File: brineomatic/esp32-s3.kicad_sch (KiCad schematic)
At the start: 27 parts, among them J19 USB_TYPE_C_16PIN, SW1 RESET, SW2 BOOT, U5 ESP32-S3-WROOM-1-N16R8, U6 USBLC6-2SC6, U7 SN74LV1T34DBV, U8 XC6210B332MR

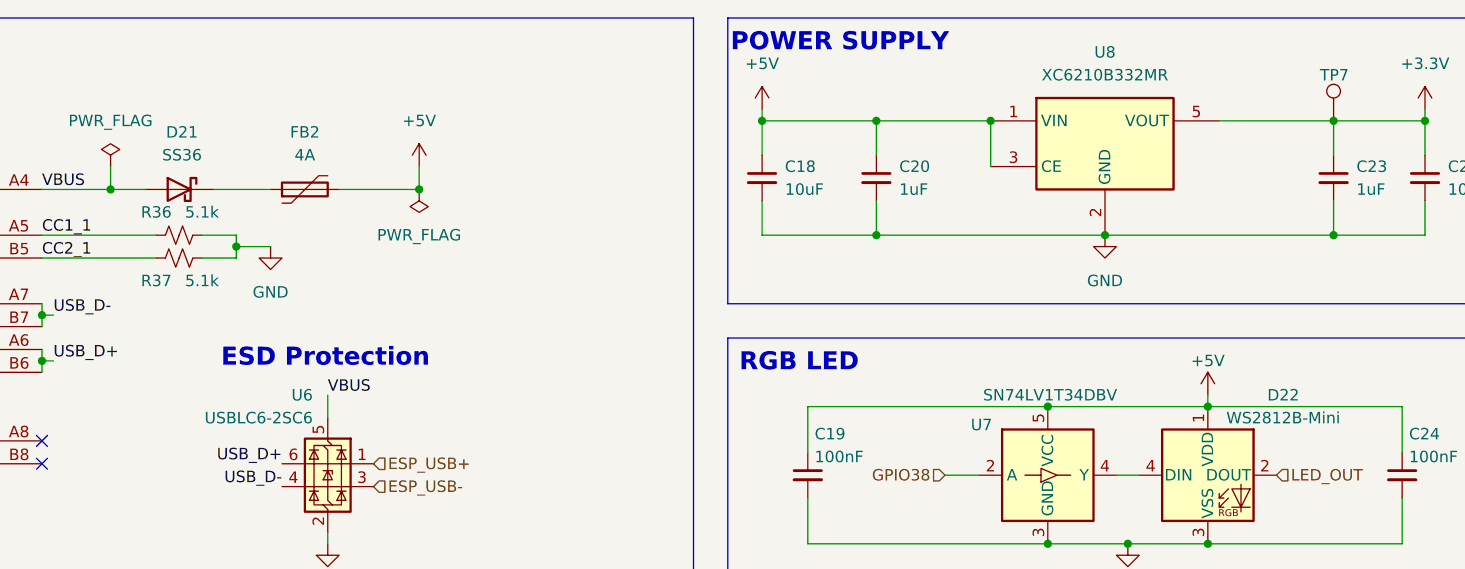
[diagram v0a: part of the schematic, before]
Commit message: more esd protection, drc passing, silkscreen fixed
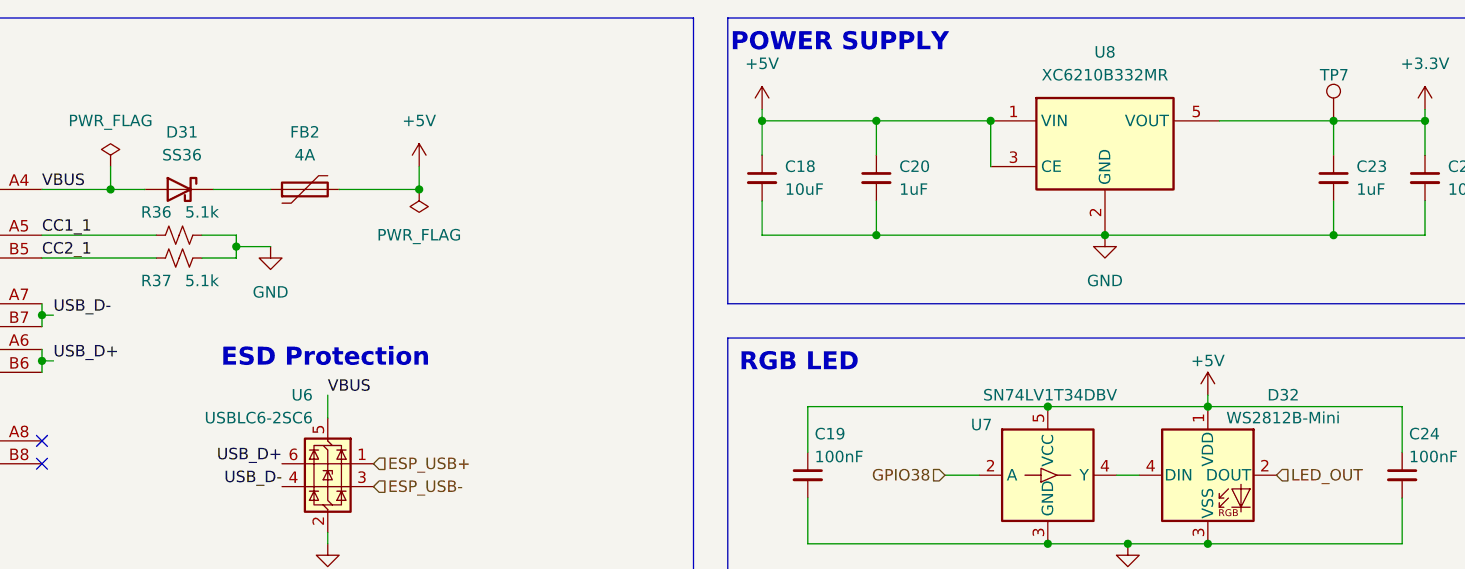
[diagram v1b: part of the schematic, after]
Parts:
- renumbered D21 to D31, D22 to D32
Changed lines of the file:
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@@
 		(on_board yes)
 		(dnp no)
-		(property "Reference" "D21"
+		(property "Reference" "D31"
 			(at 99.3775 29.21 0)
 			(effects
@@
 			(project "brineomatic"
 				(path "/96477ae2-ef08-48f3-8dd4-fe4478541f68/602af921-0504-453c-a784-e82800e98f4c"
-					(reference "D21")
+					(reference "D31")
 					(unit 1)
 				)
@@
 		(on_board yes)
 		(dnp no)
-		(property "Reference" "D22"
+		(property "Reference" "D32"
 			(at 221.742 58.42 0)
 			(effects
@@
 			(project "brineomatic"
 				(path "/96477ae2-ef08-48f3-8dd4-fe4478541f68/602af921-0504-453c-a784-e82800e98f4c"
-					(reference "D22")
-					(unit 1)
-				)
+					(reference "D32")
+					(unit 1)
+				)

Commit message: small cleanups on schematic
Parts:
- C21: value 4.7uF -> 1uF
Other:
- moved on the sheet: C18, C19, C20, C21, C22, C23, C24, C25, D32, R38, R39, SW1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

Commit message: added back up usb serial converter headers
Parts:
- added J20: Conn_01x04, Connector_PinHeader_2.54mm:PinHeader_1x04_P2.54mm_Vertical_SMD_Pin1Left, symbol Connector_Generic:Conn_01x04
- renumbered C22 to C21, C21 to C22, R39 to R38, R38 to R39, SW2 to SW1, SW1 to SW2, TP6 to TP5, TP5 to TP6
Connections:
- net +3.3V: now also J20.1 (Pin_1)
- net ESP_RXD0: now also J20.4 (Pin_4)
- net ESP_TXD0: now also J20.3 (Pin_3)
- net GND: now also J20.2 (Pin_2)
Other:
- note added: "Backup Serial Header"

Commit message: added missing gnd test point
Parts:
- renumbered TP5 to TP6, TP6 to TP7, TP7 to TP8
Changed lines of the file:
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@@
 		(on_board yes)
 		(dnp no)
-		(property "Reference" "TP7"
+		(property "Reference" "TP8"
 			(at 225.806 24.13 0)
 			(effects
@@
 			(project "brineomatic"
 				(path "/96477ae2-ef08-48f3-8dd4-fe4478541f68/602af921-0504-453c-a784-e82800e98f4c"
-					(reference "TP7")
+					(reference "TP8")
 					(unit 1)
 				)
@@
 		(on_board yes)
 		(dnp no)
-		(property "Reference" "TP6"
+		(property "Reference" "TP7"
 			(at 214.376 118.11 0)
 			(effects
@@
 			(project "brineomatic"
 				(path "/96477ae2-ef08-48f3-8dd4-fe4478541f68/602af921-0504-453c-a784-e82800e98f4c"
-					(reference "TP6")
+					(reference "TP7")
 					(unit 1)
 				)
@@
 		(on_board yes)
 		(dnp no)
-		(property "Reference" "TP5"
+		(property "Reference" "TP6"
 			(at 177.546 118.11 0)
 			(effects
@@
 			(project "brineomatic"
 				(path "/96477ae2-ef08-48f3-8dd4-fe4478541f68/602af921-0504-453c-a784-e82800e98f4c"
-					(reference "TP5")
-					(unit 1)
-				)
+					(reference "TP6")
+					(unit 1)
+				)

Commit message: added more esd protection to the power rails (24v, 5v, 3.3v)
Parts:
- added D36: SMAJ3.3A, Diode_SMD:D_SMA, symbol Device:D_TVS
- renumbered C23 to C22, C22 to C23, C25 to C24, C24 to C25, D31 to D34, D32 to D35
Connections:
- net +3.3V: now also D36.2 (A2)
- net GND: now also D36.1 (A1)
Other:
- moved on the sheet: C22, C24, TP8

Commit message: switched to the LDL1117 ldo
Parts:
- removed C18: 10uF, Capacitor_SMD:C_0603_1608Metric, symbol Device:C_Small
- removed C22: 1uF, Capacitor_SMD:C_0603_1608Metric, symbol Device:C_Small
- removed U8: XC6210B332MR, Package_TO_SOT_SMD:SOT-23-5, symbol Regulator_Linear:XC6210B332MR
- added U8: LDL1117S33R, Package_TO_SOT_SMD:SOT-223-3_TabPin2, symbol Regulator_Linear:AMS1117-3.3
- C23: renamed from C24; value 10uF -> 4.7uF
- renumbered C16 to C15, C17 to C16, C19 to C18, C20 to C19, C21 to C20, C23 to C22, C25 to C24, D34 to D33, D35 to D34, D36 to D35, R36 to R35, R37 to R36, R38 to R37, R39 to R38
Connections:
- net +3.3V: now also U8.2 (VO)
- net +5V: now also U8.3 (VI)
- net GND: now also U8.1 (GND)
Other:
- moved on the sheet: C19, C23, D35, TP8

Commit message: switch to rt7272b for 24v -> 5v regulator
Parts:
- added D34: GREEN, LED_SMD:LED_0603_1608Metric, symbol Device:LED
- added R42: 5.1k, Resistor_SMD:R_0603_1608Metric, symbol Device:R_Small_US
- D31: renamed from D33; value SS36 -> SS34; LCSC C16015 -> C8678
- renumbered C15 to C17, C16 to C18, C18 to C19, C19 to C20, C20 to C21, C23 to C22, C22 to C23, D34 to D32, D35 to D33, FB2 to FB1, R35 to R38, R36 to R39, R37 to R40, R38 to R41, TP6 to TP7, TP7 to TP9, U8 to U7, U7 to U8
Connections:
- net +3.3V: now also D34.2 (A)
- net GND: now also R42.2
- new net: D34.1 (K), R42.1
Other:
- moved on the sheet: C20, C22, D33, TP8, U7

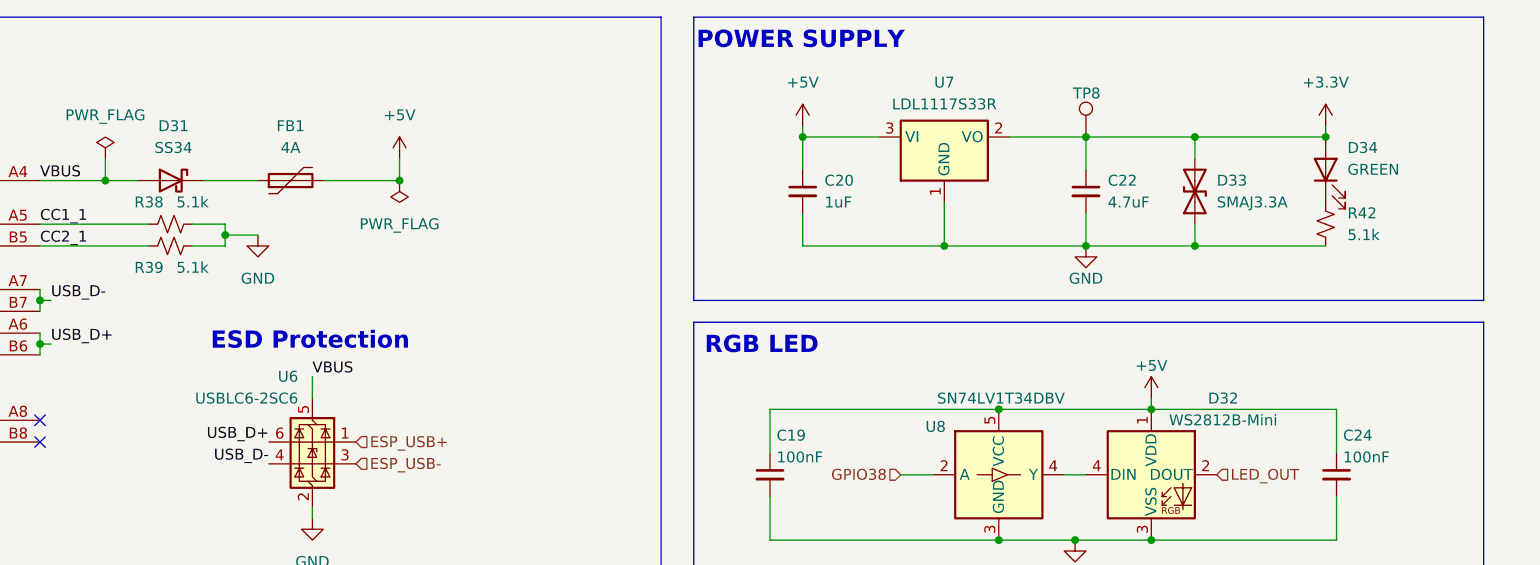
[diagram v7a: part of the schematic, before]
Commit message: added bootstrap diode just in case
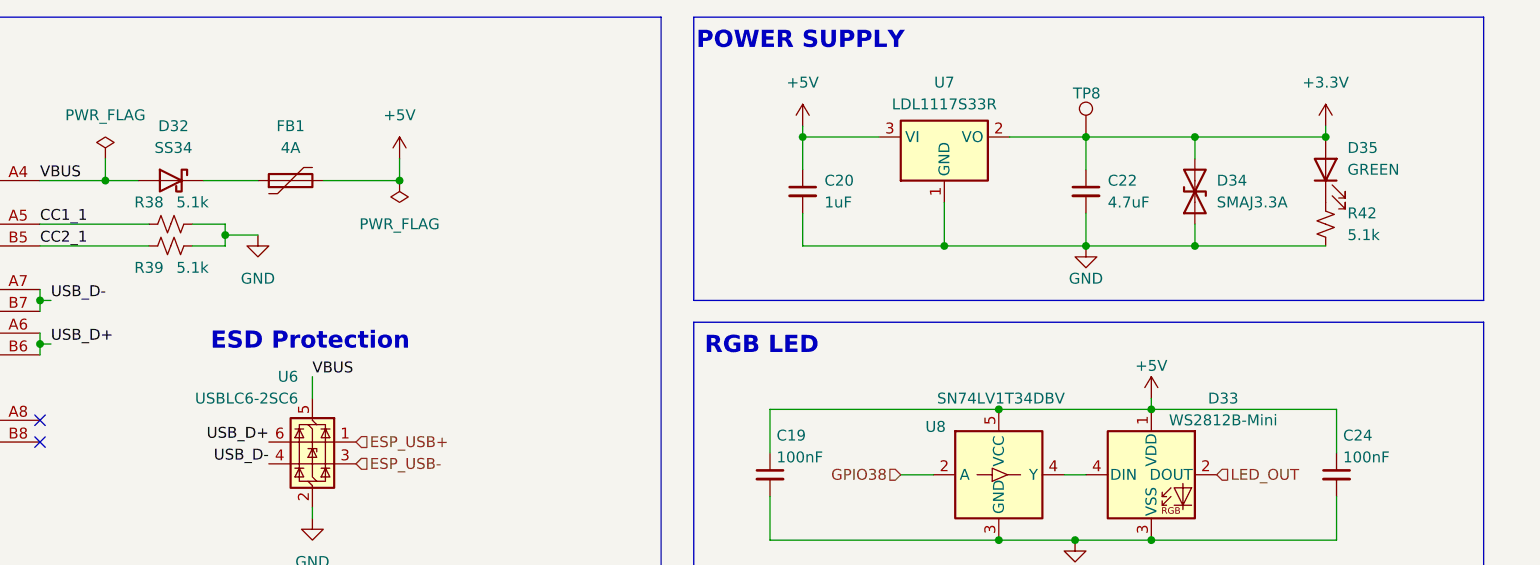
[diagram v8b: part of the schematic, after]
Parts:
- renumbered D31 to D32, D32 to D33, D33 to D34, D34 to D35
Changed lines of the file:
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@@
 		(on_board yes)
 		(dnp no)
-		(property "Reference" "#PWR045"
+		(property "Reference" "#PWR046"
 			(at 97.79 179.07 0)
 			(effects
@@
 			(project "brineomatic"
 				(path "/96477ae2-ef08-48f3-8dd4-fe4478541f68/602af921-0504-453c-a784-e82800e98f4c"
-					(reference "#PWR045")
+					(reference "#PWR046")
 					(unit 1)
 				)
@@
 		(on_board yes)
 		(dnp no)
-		(property "Reference" "#PWR057"
+		(property "Reference" "#PWR058"
 			(at 220.98 119.38 0)
 			(effects
@@
 			(project "brineomatic"
 				(path "/96477ae2-ef08-48f3-8dd4-fe4478541f68/602af921-0504-453c-a784-e82800e98f4c"
-					(reference "#PWR057")
+					(reference "#PWR058")
 					(unit 1)
 				)
@@
 		(on_board yes)
 		(dnp no)
-		(property "Reference" "D33"
+		(property "Reference" "D34"
 			(at 220.98 35.56 90)
 			(effects
@@
 			(project "brineomatic"
 				(path "/96477ae2-ef08-48f3-8dd4-fe4478541f68/602af921-0504-453c-a784-e82800e98f4c"
-					(reference "D33")
+					(reference "D34")
 					(unit 1)
 				)
@@
 		(dnp no)
 		(fields_autoplaced yes)
-		(property "Reference" "#PWR049"
+		(property "Reference" "#PWR050"
 			(at 115.57 81.28 0)
 			(effects
@@
 			(project "brineomatic"
 				(path "/96477ae2-ef08-48f3-8dd4-fe4478541f68/602af921-0504-453c-a784-e82800e98f4c"
-					(reference "#PWR049")
+					(reference "#PWR050")
 					(unit 1)
 				)
@@
 		(on_board yes)
 		(dnp no)
-		(property "Reference" "#PWR051"
+		(property "Reference" "#PWR052"
 			(at 172.72 33.02 0)
 			(effects
@@
 			(project "brineomatic"
 				(path "/96477ae2-ef08-48f3-8dd4-fe4478541f68/602af921-0504-453c-a784-e82800e98f4c"
-					(reference "#PWR051")
+					(reference "#PWR052")
 					(unit 1)
 				)
@@
 		(on_board yes)
 		(dnp no)
-		(property "Reference" "#PWR056"
+		(property "Reference" "#PWR057"
 			(at 213.36 64.77 0)
 			(effects
@@
 			(project "brineomatic"
 				(path "/96477ae2-ef08-48f3-8dd4-fe4478541f68/602af921-0504-453c-a784-e82800e98f4c"
-					(reference "#PWR056")
+					(reference "#PWR057")
 					(unit 1)
 				)
@@
 		(on_board yes)
 		(dnp no)
-		(property "Reference" "#PWR052"
+		(property "Reference" "#PWR053"
 			(at 184.15 119.38 0)
 			(effects
@@
 			(project "brineomatic"
 				(path "/96477ae2-ef08-48f3-8dd4-fe4478541f68/602af921-0504-453c-a784-e82800e98f4c"
-					(reference "#PWR052")
+					(reference "#PWR053")
 					(unit 1)
 				)
@@
 		(dnp no)
 		(fields_autoplaced yes)
-		(property "Reference" "#PWR046"
+		(property "Reference" "#PWR047"
 			(at 97.79 186.69 0)
 			(effects
@@
 			(project "brineomatic"
 				(path "/96477ae2-ef08-48f3-8dd4-fe4478541f68/602af921-0504-453c-a784-e82800e98f4c"
-					(reference "#PWR046")
+					(reference "#PWR047")
 					(unit 1)
 				)
@@
 		(dnp no)
 		(fields_autoplaced yes)
-		(property "Reference" "#PWR044"
+		(property "Reference" "#PWR045"
 			(at 85.09 162.56 0)
 			(effects
@@
 			(project "brineomatic"
 				(path "/96477ae2-ef08-48f3-8dd4-fe4478541f68/602af921-0504-453c-a784-e82800e98f4c"
-					(reference "#PWR044")
+					(reference "#PWR045")
 					(unit 1)
 				)
@@
 		(dnp no)
 		(fields_autoplaced yes)
-		(property "Reference" "#PWR054"
+		(property "Reference" "#PWR055"
 			(at 204.47 83.82 0)
 			(effects
@@
 			(project "brineomatic"
 				(path "/96477ae2-ef08-48f3-8dd4-fe4478541f68/602af921-0504-453c-a784-e82800e98f4c"
-					(reference "#PWR054")
+					(reference "#PWR055")
 					(unit 1)
 				)
@@
 		(on_board yes)
 		(dnp no)
-		(property "Reference" "D31"
+		(property "Reference" "D32"
 			(at 99.3775 29.21 0)
 			(effects
@@
 			(project "brineomatic"
 				(path "/96477ae2-ef08-48f3-8dd4-fe4478541f68/602af921-0504-453c-a784-e82800e98f4c"
-					(reference "D31")
+					(reference "D32")
 					(unit 1)
 				)
@@
 		(dnp no)
 		(fields_autoplaced yes)
-		(property "Reference" "#PWR058"
+		(property "Reference" "#PWR059"
 			(at 229.87 144.78 0)
 			(effects
@@
 			(project "brineomatic"
 				(path "/96477ae2-ef08-48f3-8dd4-fe4478541f68/602af921-0504-453c-a784-e82800e98f4c"
-					(reference "#PWR058")
+					(reference "#PWR059")
 					(unit 1)
 				)
@@
 		(dnp no)
 		(fields_autoplaced yes)
-		(property "Reference" "#PWR053"
+		(property "Reference" "#PWR054"
 			(at 193.04 143.51 0)
 			(effects
@@
 			(project "brineomatic"
 				(path "/96477ae2-ef08-48f3-8dd4-fe4478541f68/602af921-0504-453c-a784-e82800e98f4c"
-					(reference "#PWR053")
+					(reference "#PWR054")
 					(unit 1)
 				)
@@
 		(on_board yes)
 		(dnp no)
-		(property "Reference" "D32"
+		(property "Reference" "D33"
 			(at 221.742 60.96 0)
 			(effects
@@
 			(project "brineomatic"
 				(path "/96477ae2-ef08-48f3-8dd4-fe4478541f68/602af921-0504-453c-a784-e82800e98f4c"
-					(reference "D32")
+					(reference "D33")
 					(unit 1)
 				)
@@
 		(dnp no)
 		(fields_autoplaced yes)
-		(property "Reference" "#PWR048"
+		(property "Reference" "#PWR049"
 			(at 109.22 48.26 0)
 			(effects
@@
 			(project "brineomatic"
 				(path "/96477ae2-ef08-48f3-8dd4-fe4478541f68/602af921-0504-453c-a784-e82800e98f4c"
-					(reference "#PWR048")
+					(reference "#PWR049")
 					(unit 1)
 				)
@@
 		(on_board yes)
 		(dnp no)
-		(property "Reference" "#PWR047"
+		(property "Reference" "#PWR048"
 			(at 106.68 100.33 0)
 			(effects
@@
 			(project "brineomatic"
 				(path "/96477ae2-ef08-48f3-8dd4-fe4478541f68/602af921-0504-453c-a784-e82800e98f4c"
-					(reference "#PWR047")
+					(reference "#PWR048")
 					(unit 1)
 				)
@@
 		(on_board yes)
 		(dnp no)
-		(property "Reference" "#PWR059"
+		(property "Reference" "#PWR060"
 			(at 233.68 33.02 0)
 			(effects
@@
 			(project "brineomatic"
 				(path "/96477ae2-ef08-48f3-8dd4-fe4478541f68/602af921-0504-453c-a784-e82800e98f4c"
-					(reference "#PWR059")
+					(reference "#PWR060")
 					(unit 1)
 				)
@@
 		(on_board yes)
 		(dnp no)
-		(property "Reference" "D34"
+		(property "Reference" "D35"
 			(at 236.22 31.75 90)
 			(effects
@@
 			(project "brineomatic"
 				(path "/96477ae2-ef08-48f3-8dd4-fe4478541f68/602af921-0504-453c-a784-e82800e98f4c"
-					(reference "D34")
+					(reference "D35")
 					(unit 1)
 				)
@@
 		(dnp no)
 		(fields_autoplaced yes)
-		(property "Reference" "#PWR043"
+		(property "Reference" "#PWR044"
 			(at 64.77 80.01 0)
 			(effects
@@
 			(project "brineomatic"
 				(path "/96477ae2-ef08-48f3-8dd4-fe4478541f68/602af921-0504-453c-a784-e82800e98f4c"
-					(reference "#PWR043")
+					(reference "#PWR044")
 					(unit 1)
 				)
@@
 		(on_board yes)
 		(dnp no)
-		(property "Reference" "#PWR050"
+		(property "Reference" "#PWR051"
 			(at 125.73 36.83 0)
 			(effects
@@
 			(project "brineomatic"
 				(path "/96477ae2-ef08-48f3-8dd4-fe4478541f68/602af921-0504-453c-a784-e82800e98f4c"
-					(reference "#PWR050")
+					(reference "#PWR051")
 					(unit 1)
 				)
@@
 		(on_board yes)
 		(dnp no)
-		(property "Reference" "#PWR055"
+		(property "Reference" "#PWR056"
 			(at 205.74 49.53 0)
 			(effects
@@
 			(project "brineomatic"
 				(path "/96477ae2-ef08-48f3-8dd4-fe4478541f68/602af921-0504-453c-a784-e82800e98f4c"
-					(reference "#PWR055")
+					(reference "#PWR056")
 					(unit 1)
 				)
